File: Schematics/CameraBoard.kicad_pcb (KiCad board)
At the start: 2 copper layers, 62.6 x 53 mm, 61 parts, among them J2 USB_C_Receptacle, U1 STM32F405RGTx, U2 TPS22917DBVR, U3 TPS22917DBVR, U4 SN65HVD230DR, U5 AMS1117-3.3, U6 TPS22917DBVR

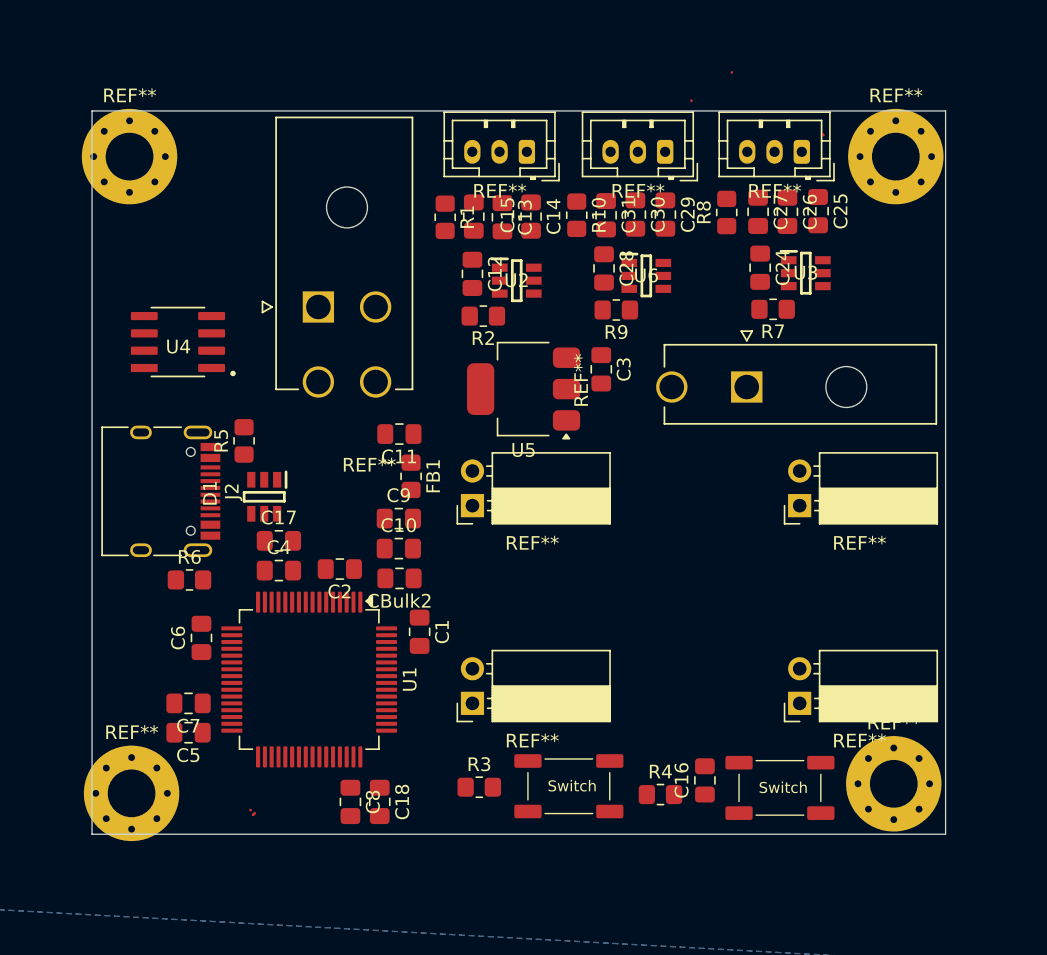
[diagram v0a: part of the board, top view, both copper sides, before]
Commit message: replaced items under buck module almost ready for routing
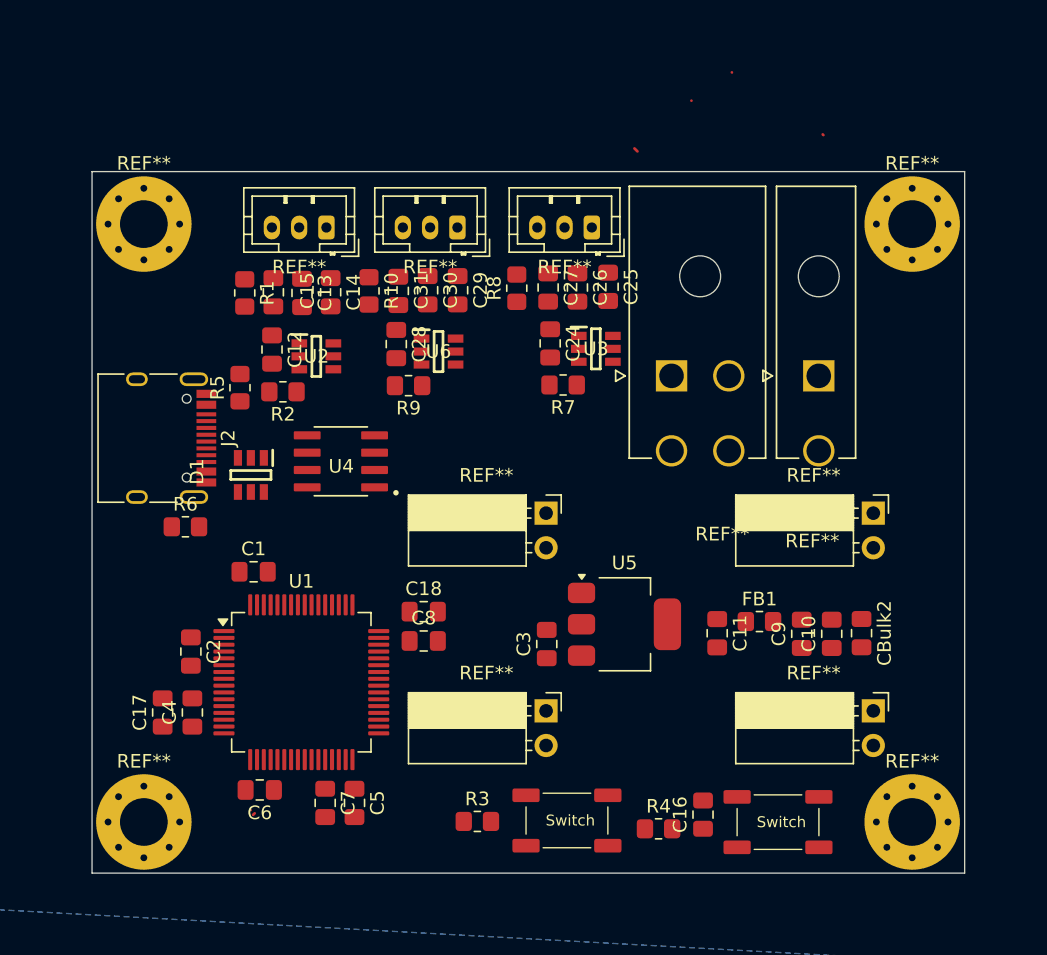
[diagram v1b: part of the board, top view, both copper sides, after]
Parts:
- moved CBulk2 34.1 mm to (108.8, 97.6), turned to -90 degrees
- moved REF** 33.0 mm to (109.7, 103.3), turned to 0 degrees
- moved REF** 32.5 mm to (109.7, 88.8), turned to 0 degrees
- moved C10 32.4 mm to (106.7, 97.7), turned to 90 degrees
- moved C9 30.7 mm to (104.5, 97.7), turned to 90 degrees
- moved FB1 27.7 mm to (101.3, 96.8), turned to 0 degrees
- moved C11 27.5 mm to (98.2, 97.6), turned to -90 degrees
- moved REF** 26.4 mm to (94.9, 78.7)
- moved REF** 23.9 mm to (85.7, 103.3), turned to 0 degrees
- moved REF** 23.2 mm to (85.7, 88.8), turned to 0 degrees
- moved C3 20.5 mm to (85.8, 98.4), turned to 90 degrees
- moved U5 18.8 mm to (91.5, 97.0), turned to 0 degrees
- moved C24 16.4 mm to (86.0, 76.3)
- moved C25 16.4 mm to (90.2, 72.2)
- moved C26 16.4 mm to (88.0, 72.2)
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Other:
- board size 62.6 x 53 mm -> 64 x 51.5 mm

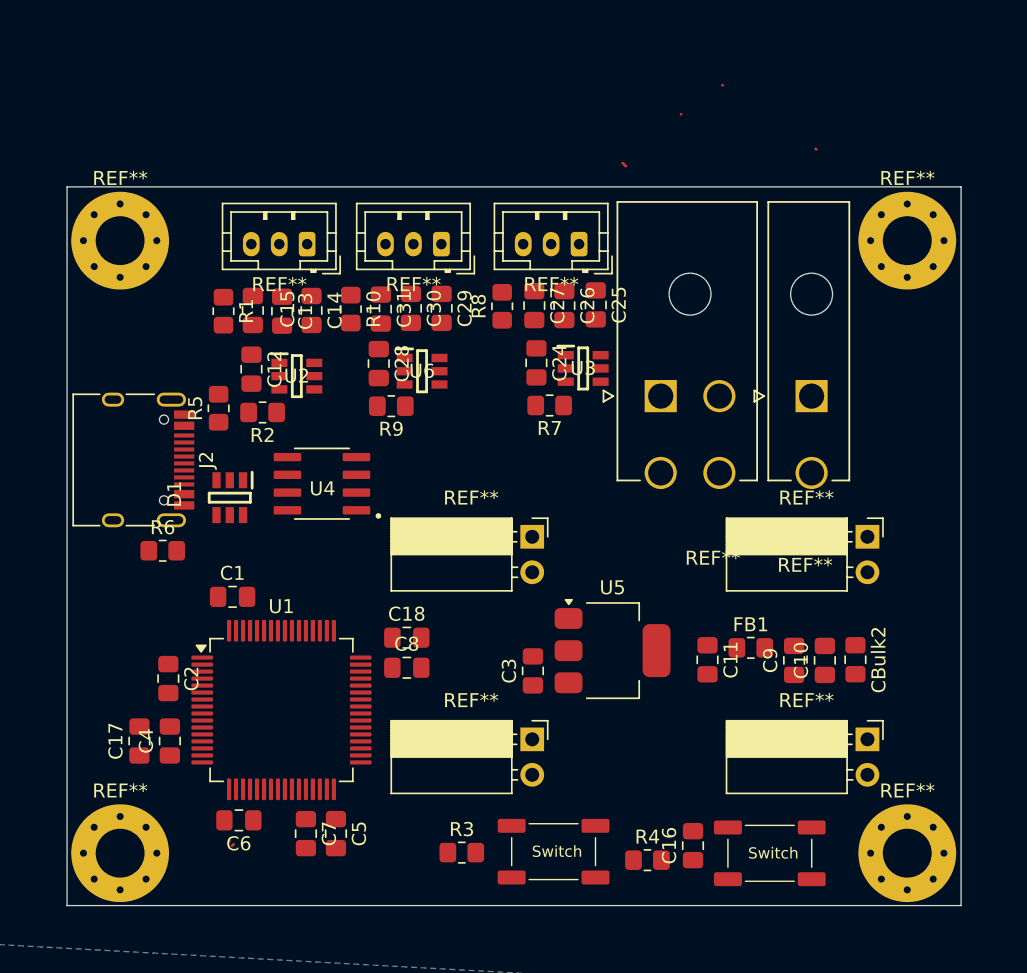
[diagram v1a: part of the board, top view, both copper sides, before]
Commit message: Fixed Schematic and PCB refrences everything is connected correctly now
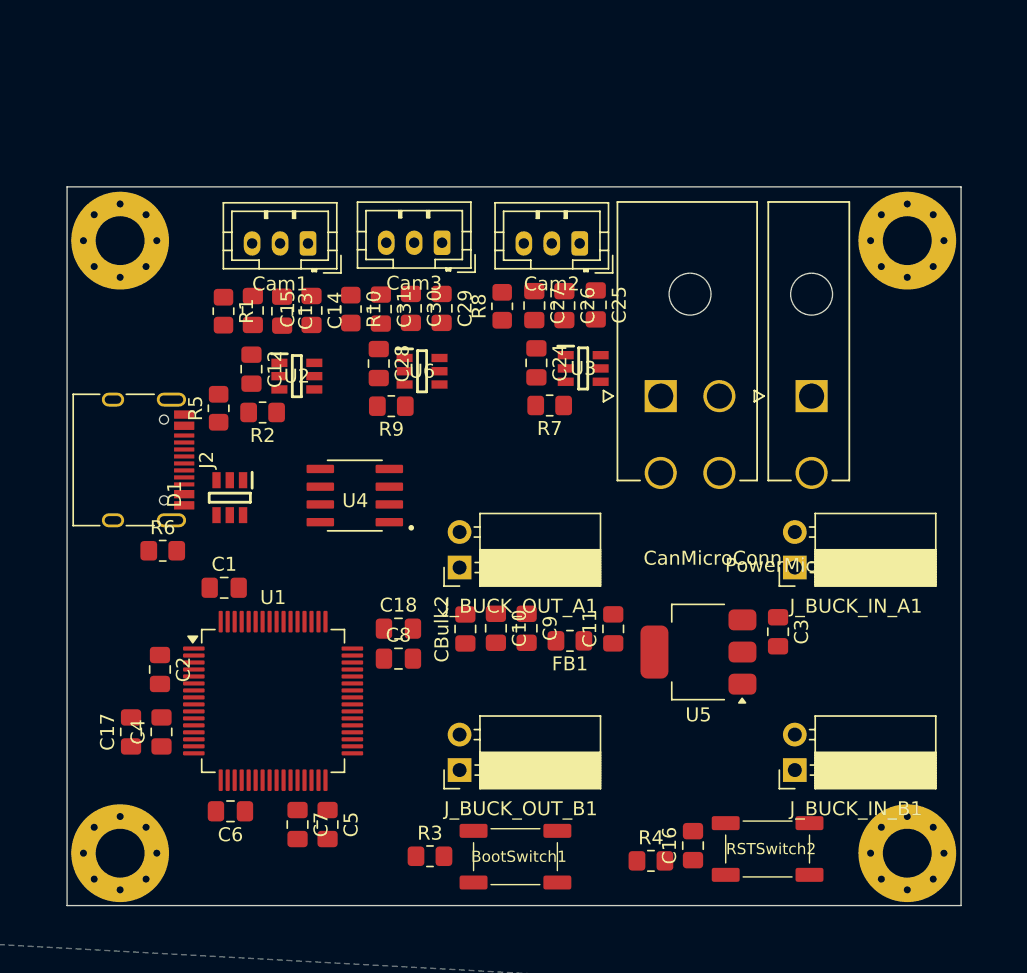
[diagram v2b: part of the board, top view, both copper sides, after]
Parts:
- removed REF** (x3): JST_PH_B3B-PH-K_1x03_P2.00mm_Vertical, Connector_JST:JST_PH_B3B-PH-K_1x03_P2.00mm_Vertical
- removed REF** (x4): PinSocket_1x02_P2.54mm_Horizontal, Connector_PinSocket_2.54mm:PinSocket_1x02_P2.54mm_Horizontal
- removed Switch (x2): SAMZO G4R0015010, Button_Switch_THT:SAMZO G4R0015010
- added BootSwitch1: SAMZO G4R0015010, myFootprints:SAMZO G4R0015010, F.Cu at (84.5, 111.7)
- added Cam1: Conn_01x03, Connector_JST:JST_PH_B3B-PH-K_1x03_P2.00mm_Vertical, F.Cu at (69.7, 67.8)
- added Cam2: Conn_01x03, Connector_JST:JST_PH_B3B-PH-K_1x03_P2.00mm_Vertical, F.Cu at (89.1, 67.8)
- added Cam3: Conn_01x03, Connector_JST:JST_PH_B3B-PH-K_1x03_P2.00mm_Vertical, F.Cu at (79.2, 67.8)
- added J_BUCK_IN_A1: ~, Connector_PinSocket_2.54mm:PinSocket_1x02_P2.54mm_Horizontal, F.Cu at (104.5, 91.0)
- added J_BUCK_IN_B1: ~, Connector_PinSocket_2.54mm:PinSocket_1x02_P2.54mm_Horizontal, F.Cu at (104.5, 105.5)
- added J_BUCK_OUT_A1: ~, Connector_PinSocket_2.54mm:PinSocket_1x02_P2.54mm_Horizontal, F.Cu at (80.5, 91.0)
- added J_BUCK_OUT_B1: ~, Connector_PinSocket_2.54mm:PinSocket_1x02_P2.54mm_Horizontal, F.Cu at (80.5, 105.5)
- added RSTSwitch2: SAMZO G4R0015010, myFootprints:SAMZO G4R0015010, F.Cu at (102.5, 111.2)
- moved CBulk2 28.0 mm to (80.9, 95.4), turned to 90 degrees
- moved C10 23.7 mm to (83.1, 95.3), turned to -90 degrees
- moved C9 19.3 mm to (85.3, 95.3), turned to -90 degrees
- moved C3 17.8 mm to (103.3, 95.6), turned to -90 degrees
- moved FB1 13.0 mm to (88.4, 96.2), turned to 180 degrees
- moved C11 7.10 mm to (91.5, 95.4), turned to 90 degrees
- moved U5 6.15 mm to (97.6, 97.0), turned to 180 degrees
- moved U4 2.50 mm to (73.0, 85.8)
- moved R3 2.29 mm to (78.4, 111.7)
- moved C17 0.88 mm to (57.0, 102.8)
- moved C2 0.88 mm to (59.0, 98.3)
- moved C4 0.88 mm to (59.2, 102.8)
- moved C18 0.88 mm to (76.1, 95.4)
- moved U1 0.88 mm to (67.2, 100.5)
- moved C5 0.88 mm to (71.0, 109.4)
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- renumbered REF** to CanMicroConn, REF** to MountingHole, REF** to Mountinghole, REF** to PowerMicroConn
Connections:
- C16 pad 2: Net-(C16-Pad2) -> unconnected-(C16-Pad2)

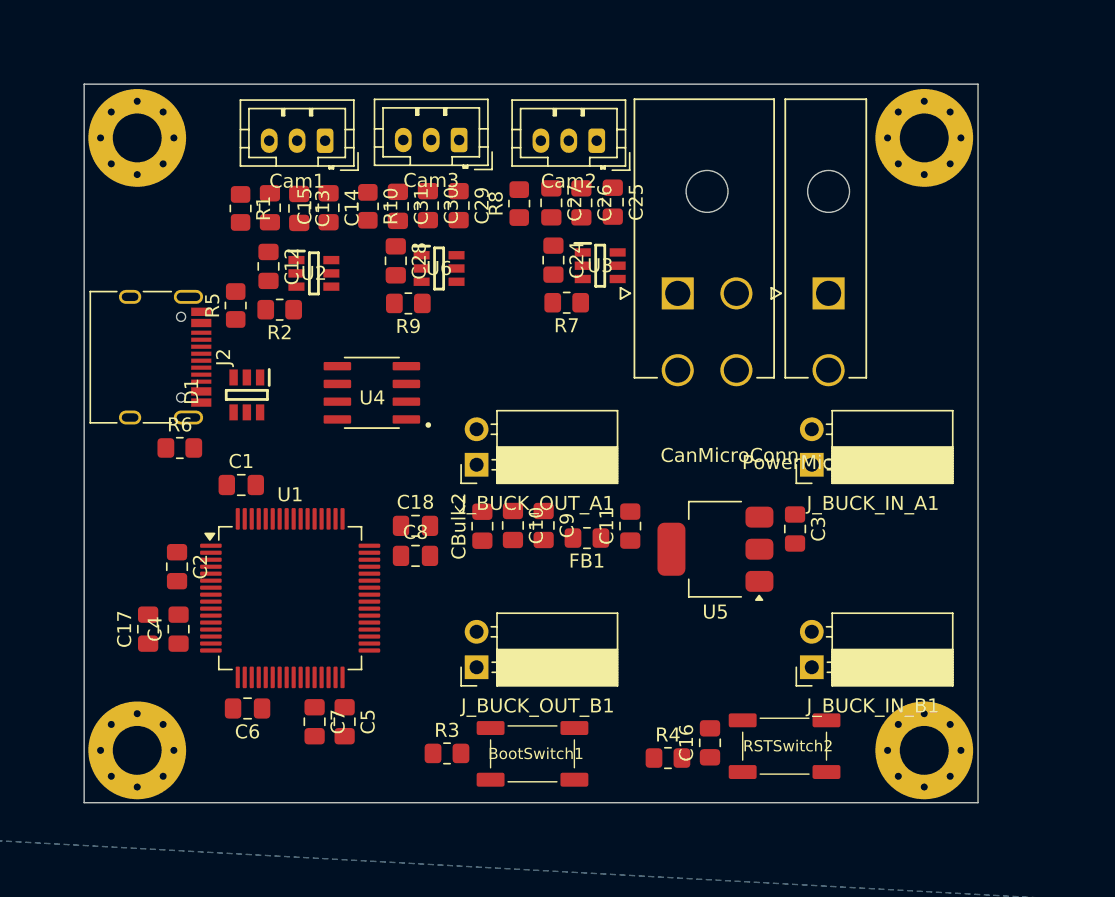
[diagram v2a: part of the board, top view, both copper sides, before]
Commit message: fixed all refrences from shematic to pcb and added LED
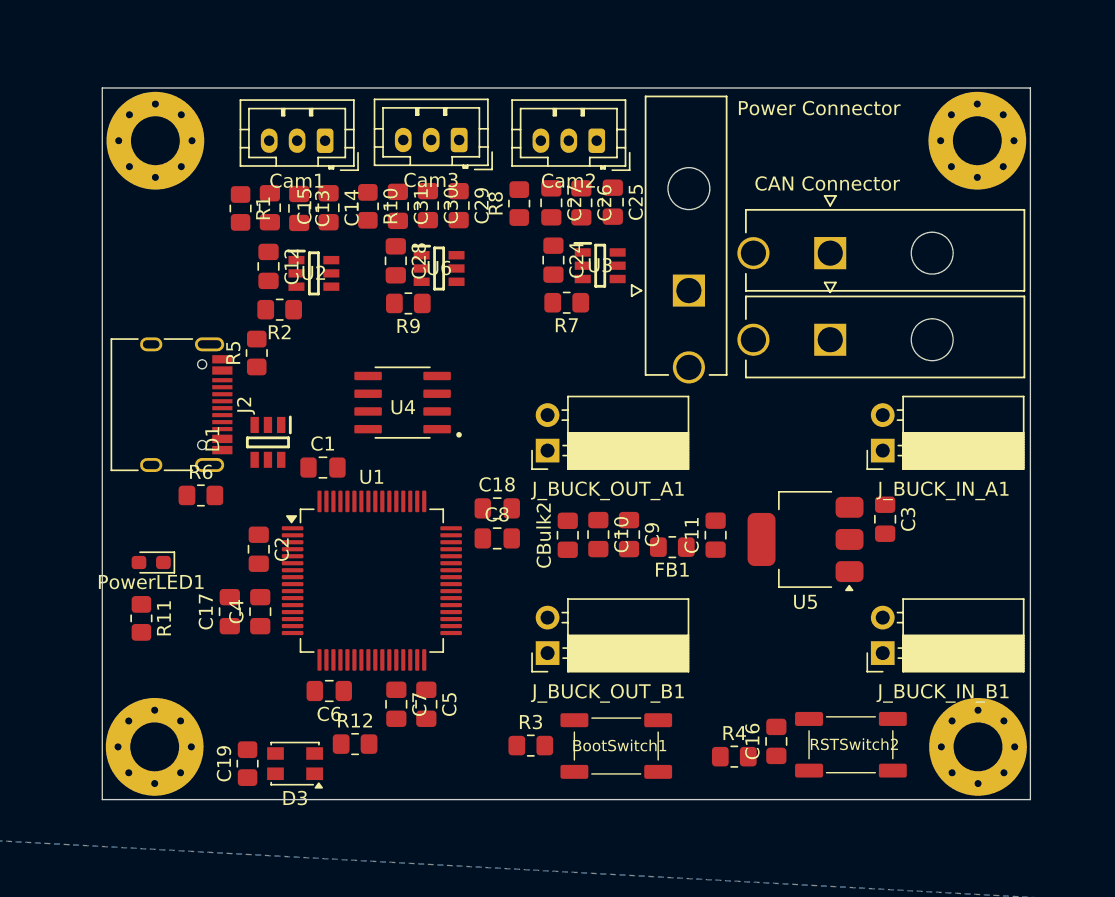
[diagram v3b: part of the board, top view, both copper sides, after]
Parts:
- removed CanMicroConn: MOLEX_26013115, myFootprints:MOLEX_26013115
- added C19: 100nf, Resistor_SMD:R_0805_2012Metric_Pad1.20x1.40mm_HandSolder, F.Cu at (64.1, 112.4)
- added CAN Connector: MOLEX_26013114, myFootprints:MOLEX_26013114, F.Cu at (105.8, 75.8)
- added D3: NeoPixel_THT, LED_SMD:LED_Kingbright_AAA3528ESGCT, F.Cu at (67.5, 112.4)
- added PowerLED1: RLED, LED_SMD:LED_0603_1608Metric_Pad1.05x0.95mm_HandSolder, F.Cu at (57.2, 98.0)
- added PowerMicroConn: MOLEX_26013114, myFootprints:MOLEX_26013114, F.Cu at (105.8, 82.0)
- added R11: 1k, Resistor_SMD:R_0805_2012Metric_Pad1.20x1.40mm_HandSolder, F.Cu at (56.5, 102.0)
- added R12: .33k, Resistor_SMD:R_0805_2012Metric_Pad1.20x1.40mm_HandSolder, F.Cu at (71.8, 111.0)
- Power Connector: renamed from PowerMicroConn
- moved Power Connector 10.0 mm to (95.7, 78.5)
- moved U5 6.49 mm to (104.0, 96.3)
- moved C3 6.49 mm to (109.8, 94.9)
- moved C10 6.15 mm to (89.2, 96.0)
- moved CBulk2 6.15 mm to (87.0, 96.0)
- moved C11 6.15 mm to (97.6, 96.0)
- moved C9 6.15 mm to (91.4, 96.0)
- moved FB1 6.15 mm to (94.5, 96.9)
- moved BootSwitch1 6.03 mm to (90.5, 111.1)
- moved R3 6.03 mm to (84.4, 111.1)
- moved C2 5.98 mm to (64.9, 97.0)
- moved C4 5.98 mm to (65.0, 101.5)
- moved C5 5.98 mm to (76.9, 108.2)
- moved C6 5.98 mm to (70.0, 107.2)
- moved C1 5.98 mm to (69.5, 91.2)
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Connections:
- C16 pad 2: unconnected-(C16-Pad2) -> Net-(C16-Pad2)
- RSTSwitch2 pad 1: unconnected-(RSTSwitch2-Pad1) -> GND
- RSTSwitch2 pad 2: unconnected-(RSTSwitch2-Pad2) -> Net-(C16-Pad2)
- U1 pad 24: unconnected-(U1-PC4-Pad24) -> /MCU/RGB_DATA
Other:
- board size 64 x 51.5 mm -> 66.5 x 50.9 mm

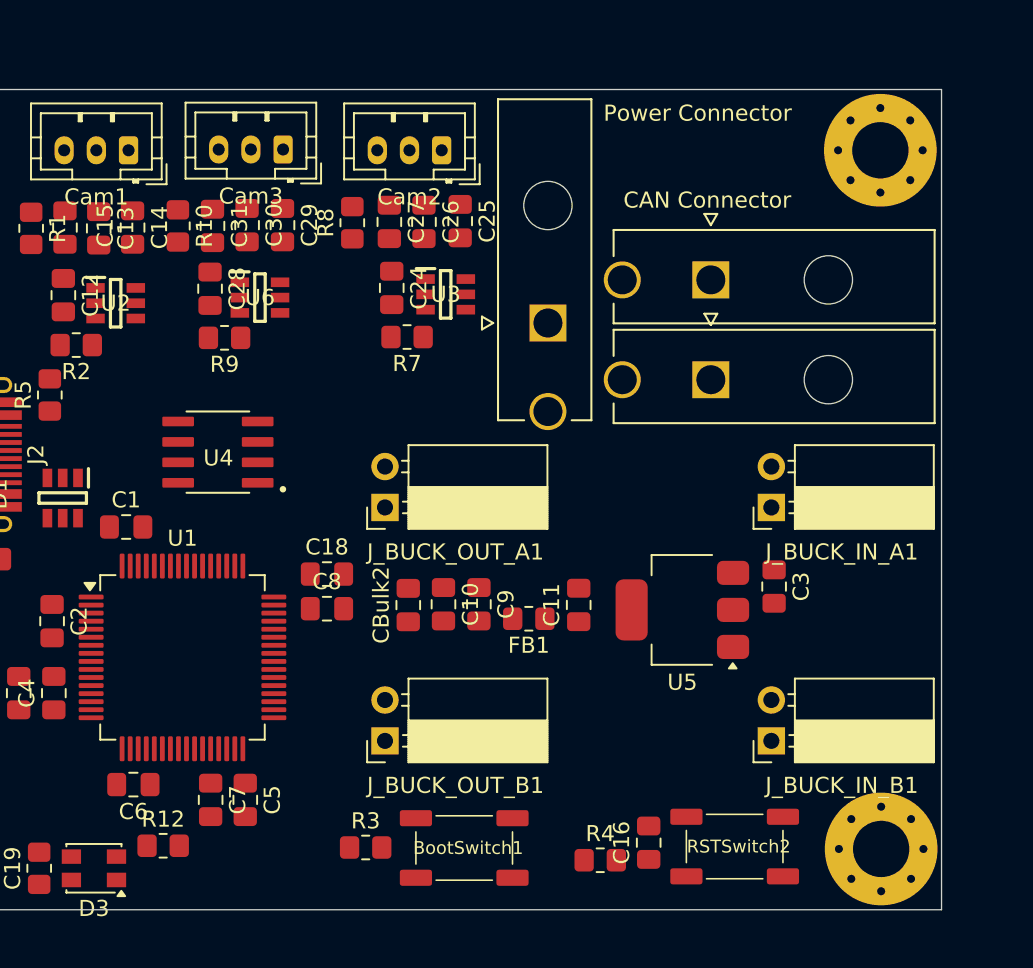
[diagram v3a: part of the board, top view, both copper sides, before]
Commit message: all nets are correct within PCB and correct CAN is implemented
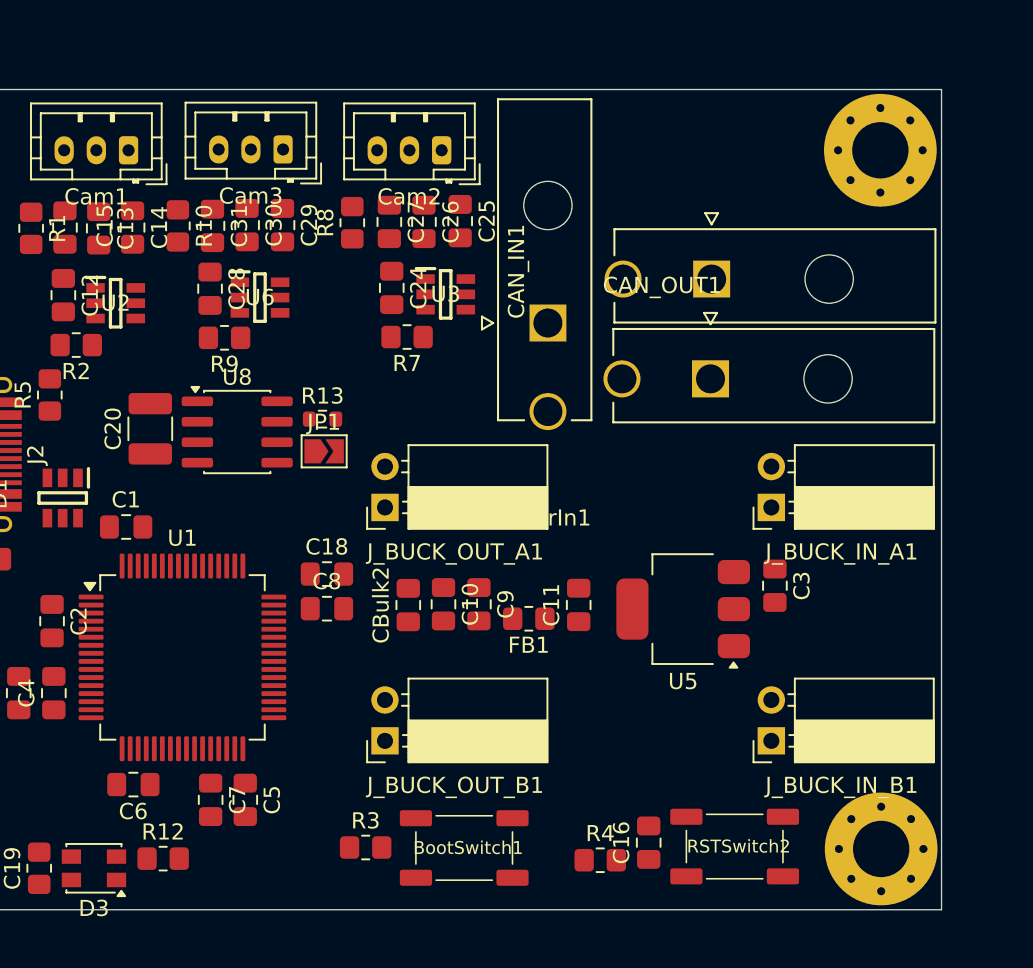
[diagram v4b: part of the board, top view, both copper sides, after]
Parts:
- removed CAN Connector: MOLEX_26013114, myFootprints:MOLEX_26013114
- removed Power Connector: MOLEX_26013114, myFootprints:MOLEX_26013114
- removed PowerMicroConn: MOLEX_26013114, myFootprints:MOLEX_26013114
- removed U4: SN65HVD230DR, myFootprints:SOIC127P599X175-8N
- added C20: 100nF, Capacitor_SMD:C_1210_3225Metric_Pad1.33x2.70mm_HandSolder, F.Cu at (71.0, 85.1)
- added CAN_IN1: ~, myFootprints:MOLEX_26013114, F.Cu at (105.9, 75.8)
- added CAN_OUT1: ~, myFootprints:MOLEX_26013114, F.Cu at (105.8, 82.0)
- added JP1: SolderJumper_2_Open, Jumper:SolderJumper-2_P1.3mm_Open_TrianglePad1.0x1.5mm, F.Cu at (81.8, 86.5)
- added PowerIn1: ~, myFootprints:MOLEX_26013114, F.Cu at (95.7, 78.5)
- added R13: 120R, Resistor_SMD:R_0603_1608Metric, F.Cu at (81.7, 84.5)
- added U8: SN65HVD230, Package_SO:SOIC-8_3.9x4.9mm_P1.27mm, F.Cu at (76.4, 85.3)
- moved R12 0.80 mm to (71.8, 111.8)
- moved C3 0.07 mm to (109.8, 94.8)
- moved U5 0.07 mm to (104.1, 96.3)
